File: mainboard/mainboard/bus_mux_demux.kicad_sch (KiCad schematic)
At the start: 10 parts

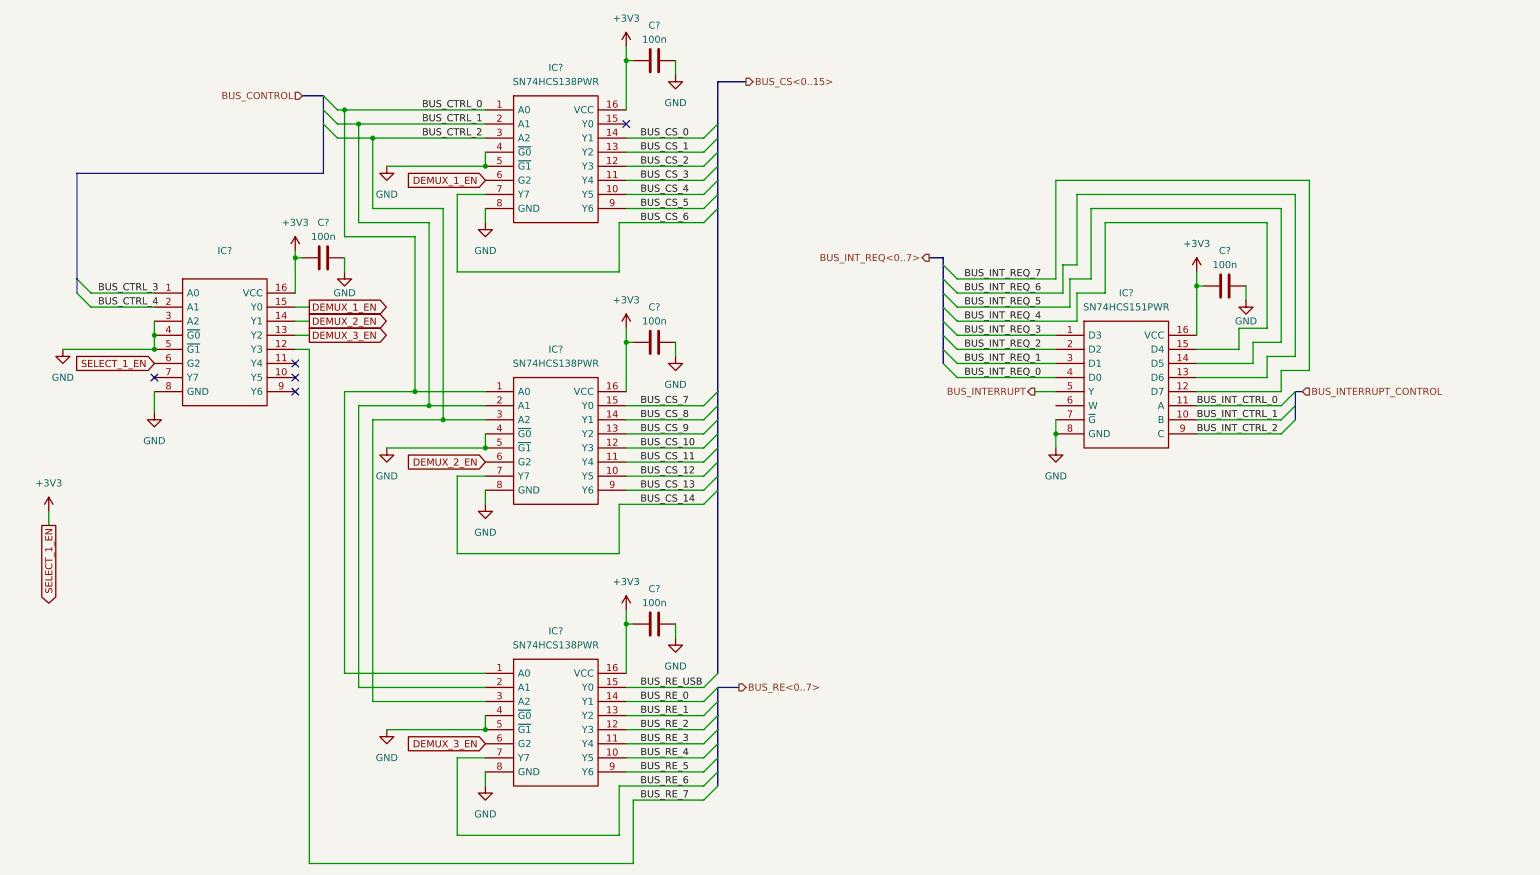
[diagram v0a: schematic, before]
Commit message: Fixing labels
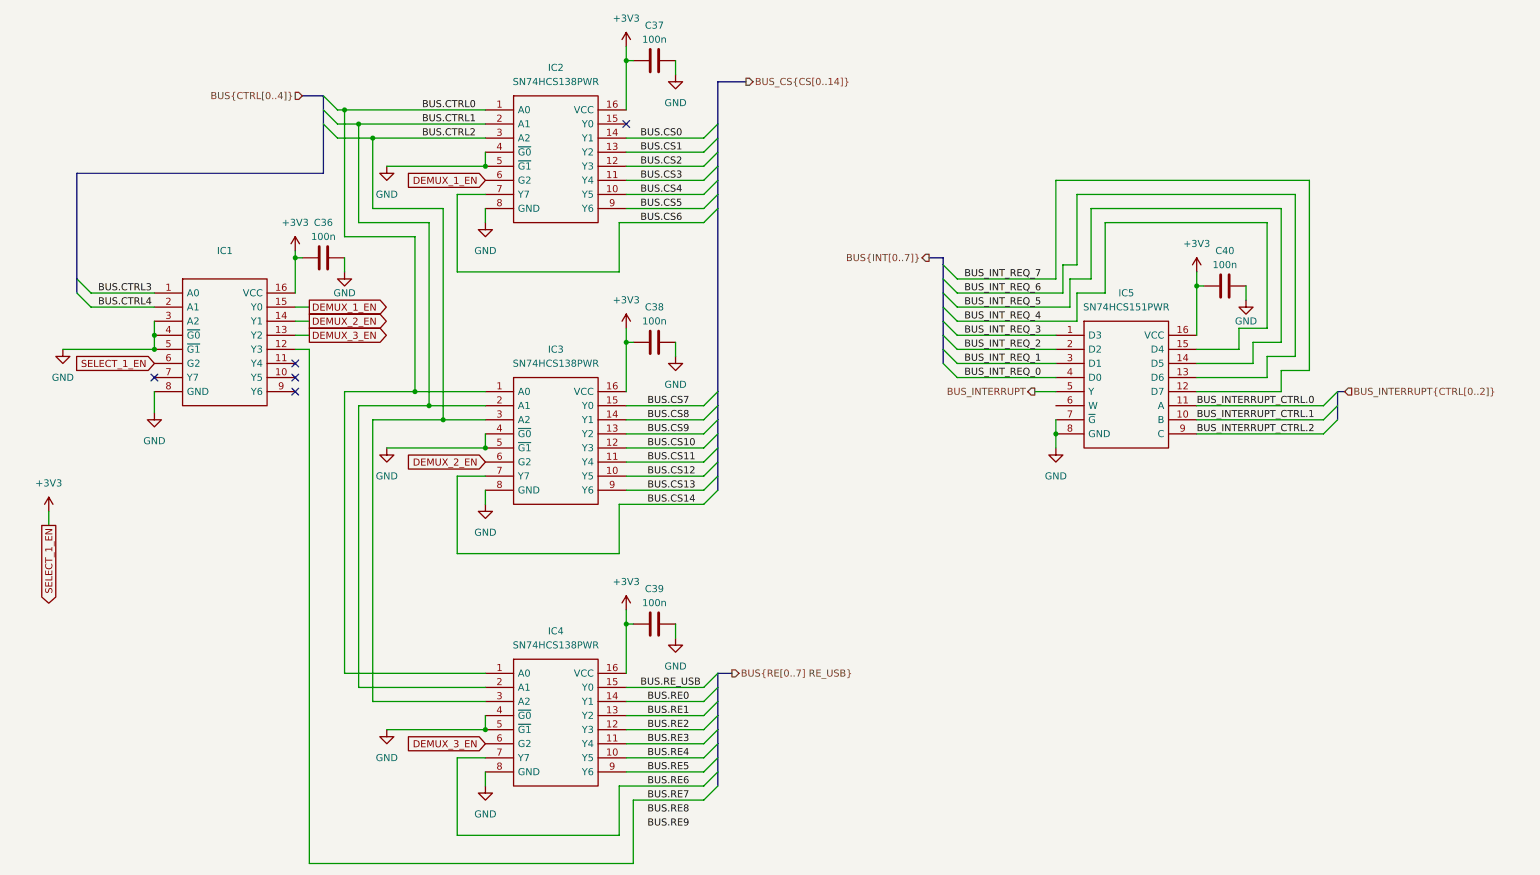
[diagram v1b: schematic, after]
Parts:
- gave numbers to parts that had none: 10
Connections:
- net BUS_CS_0 renamed BUS.CS0
- net BUS_CS_1 renamed BUS.CS1
- net BUS_CS_10 renamed BUS.CS10
- net BUS_CS_11 renamed BUS.CS11
- net BUS_CS_12 renamed BUS.CS12
- net BUS_CS_13 renamed BUS.CS13
- net BUS_CS_14 renamed BUS.CS14
- net BUS_CS_2 renamed BUS.CS2
- net BUS_CS_3 renamed BUS.CS3
- net BUS_CS_4 renamed BUS.CS4
- net BUS_CS_5 renamed BUS.CS5
- net BUS_CS_6 renamed BUS.CS6
- net BUS_CS_7 renamed BUS.CS7
- net BUS_CS_8 renamed BUS.CS8
- net BUS_CS_9 renamed BUS.CS9
- net BUS_CTRL_0 renamed BUS.CTRL0
- net BUS_CTRL_1 renamed BUS.CTRL1
- net BUS_CTRL_2 renamed BUS.CTRL2
- net BUS_CTRL_3 renamed BUS.CTRL3
- net BUS_CTRL_4 renamed BUS.CTRL4
- net BUS_INT_CTRL_0 renamed BUS_INTERRUPT_CTRL.0
- net BUS_INT_CTRL_1 renamed BUS_INTERRUPT_CTRL.1
- net BUS_INT_CTRL_2 renamed BUS_INTERRUPT_CTRL.2
- net BUS_RE_0 renamed BUS.RE0
- net BUS_RE_1 renamed BUS.RE1
- net BUS_RE_2 renamed BUS.RE2
- net BUS_RE_3 renamed BUS.RE3
- net BUS_RE_4 renamed BUS.RE4
- net BUS_RE_5 renamed BUS.RE5
- net BUS_RE_6 renamed BUS.RE6
- net BUS_RE_7 renamed BUS.RE7
- net BUS_RE_USB renamed BUS.RE_USB

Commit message: fixed warnings and errors
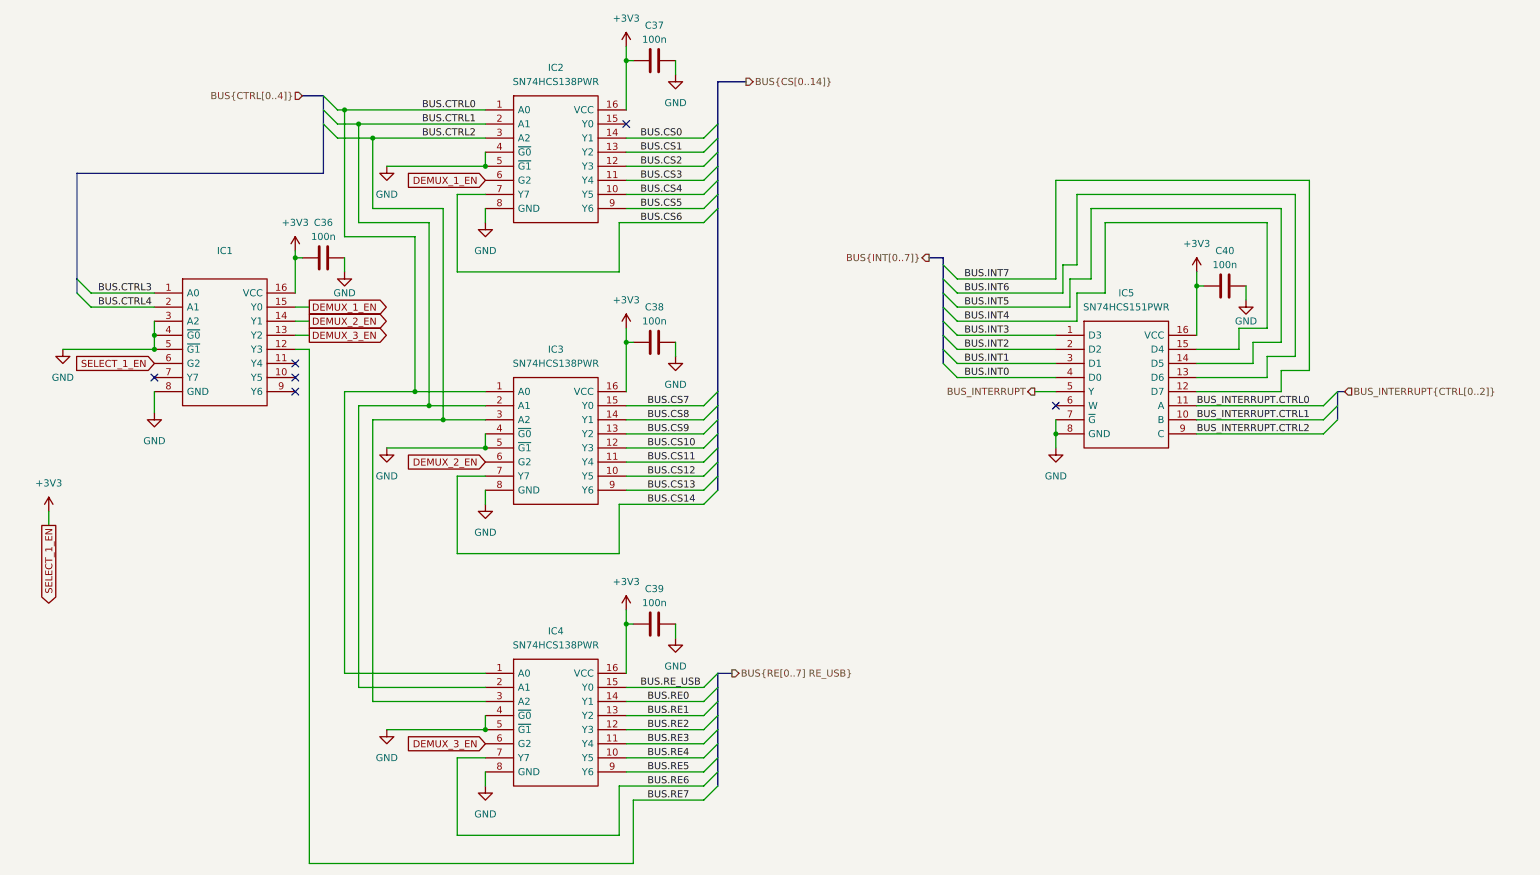
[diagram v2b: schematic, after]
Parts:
- IC1: footprint (none) -> SOP65P640X120-16N
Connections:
- net BUS_INTERRUPT_CTRL.0 renamed BUS_INTERRUPT.CTRL0
- net BUS_INTERRUPT_CTRL.1 renamed BUS_INTERRUPT.CTRL1
- net BUS_INTERRUPT_CTRL.2 renamed BUS_INTERRUPT.CTRL2
- net BUS_INT_REQ_0 renamed BUS.INT0
- net BUS_INT_REQ_1 renamed BUS.INT1
- net BUS_INT_REQ_2 renamed BUS.INT2
- net BUS_INT_REQ_3 renamed BUS.INT3
- net BUS_INT_REQ_4 renamed BUS.INT4
- net BUS_INT_REQ_5 renamed BUS.INT5
- net BUS_INT_REQ_6 renamed BUS.INT6
- net BUS_INT_REQ_7 renamed BUS.INT7
- no-connect marks 5 -> 6
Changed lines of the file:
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@@
   )
   (no_connect (at 132.08 39.37))
+  (no_connect (at 209.55 90.17))
   (no_connect (at 72.39 87.63))
   (no_connect (at 72.39 85.09))
@@
     (stroke (width 0) (type default) (color 0 0 0 0))
   )
-  (label "BUS_INT_REQ_2" (at 193.04 80.01 0)
+  (label "BUS.INT2" (at 193.04 80.01 0)
     (effects (font (size 1.27 1.27)) (justify left bottom))
   )
@@
     (effects (font (size 1.27 1.27)) (justify left bottom))
   )
-  (label "BUS_INT_REQ_4" (at 193.04 74.93 0)
+  (label "BUS.INT4" (at 193.04 74.93 0)
     (effects (font (size 1.27 1.27)) (justify left bottom))
   )
@@
     (effects (font (size 1.27 1.27)) (justify left bottom))
   )
-  (label "BUS_INTERRUPT_CTRL.1" (at 234.95 92.71 0)
-    (effects (font (size 1.27 1.27)) (justify left bottom))
-  )
-  (label "BUS_INT_REQ_1" (at 193.04 82.55 0)
-    (effects (font (size 1.27 1.27)) (justify left bottom))
-  )
-  (label "BUS_INT_REQ_6" (at 193.04 69.85 0)
+  (label "BUS_INTERRUPT.CTRL1" (at 234.95 92.71 0)
+    (effects (font (size 1.27 1.27)) (justify left bottom))
+  )
+  (label "BUS.INT1" (at 193.04 82.55 0)
+    (effects (font (size 1.27 1.27)) (justify left bottom))
+  )
+  (label "BUS.INT6" (at 193.04 69.85 0)
     (effects (font (size 1.27 1.27)) (justify left bottom))
   )
@@
     (effects (font (size 1.27 1.27)) (justify left bottom))
   )
-  (label "BUS_INT_REQ_0" (at 193.04 85.09 0)
+  (label "BUS.INT0" (at 193.04 85.09 0)
     (effects (font (size 1.27 1.27)) (justify left bottom))
   )
@@
     (effects (font (size 1.27 1.27)) (justify left bottom))
   )
-  (label "BUS_INTERRUPT_CTRL.0" (at 234.95 90.17 0)
+  (label "BUS_INTERRUPT.CTRL0" (at 234.95 90.17 0)
     (effects (font (size 1.27 1.27)) (justify left bottom))
   )
@@
     (effects (font (size 1.27 1.27)) (justify left bottom))
   )
-  (label "BUS.RE8" (at 135.89 163.83 0)
-    (effects (font (size 1.27 1.27)) (justify left bottom))
-  )
   (label "BUS.CTRL4" (at 36.83 72.39 0)
     (effects (font (size 1.27 1.27)) (justify left bottom))
@@
     (effects (font (size 1.27 1.27)) (justify left bottom))
   )
-  (label "BUS_INT_REQ_3" (at 193.04 77.47 0)
+  (label "BUS.INT3" (at 193.04 77.47 0)
     (effects (font (size 1.27 1.27)) (justify left bottom))
   )
@@
     (effects (font (size 1.27 1.27)) (justify left bottom))
   )
-  (label "BUS_INTERRUPT_CTRL.2" (at 234.95 95.25 0)
+  (label "BUS_INTERRUPT.CTRL2" (at 234.95 95.25 0)
     (effects (font (size 1.27 1.27)) (justify left bottom))
   )
@@
     (effects (font (size 1.27 1.27)) (justify left bottom))
   )
-  (label "BUS_INT_REQ_7" (at 193.04 67.31 0)
+  (label "BUS.INT7" (at 193.04 67.31 0)
     (effects (font (size 1.27 1.27)) (justify left bottom))
   )
@@
     (effects (font (size 1.27 1.27)) (justify left bottom))
   )
-  (label "BUS.RE9" (at 135.89 166.37 0)
-    (effects (font (size 1.27 1.27)) (justify left bottom))
-  )
   (label "BUS.RE_USB" (at 134.62 140.97 0)
     (effects (font (size 1.27 1.27)) (justify left bottom))
   )
-  (label "BUS_INT_REQ_5" (at 193.04 72.39 0)
+  (label "BUS.INT5" (at 193.04 72.39 0)
     (effects (font (size 1.27 1.27)) (justify left bottom))
   )
@@
     (effects (font (size 1.27 1.27)) (justify left))
   )
-  (hierarchical_label "BUS_CS{CS[0..14]}" (shape output) (at 153.67 31.75 0)
+  (hierarchical_label "BUS{CS[0..14]}" (shape output) (at 153.67 31.75 0)
     (effects (font (size 1.27 1.27)) (justify left))
   )
@@
     (property "Reference" "IC1" (id 0) (at 59.69 62.23 0))
     (property "Value" "~" (id 1) (at 59.69 64.77 0))
-    (property "Footprint" "" (id 2) (at 68.58 67.31 0)
-      (effects (font (size 1.27 1.27)) (justify left) hide)
-    )
+    (property "Footprint" "SOP65P640X120-16N" (id 2) (at 68.58 67.31 0)
+      (effects (font (size 1.27 1.27)) (justify left) hide)
+    )

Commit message: board almost ready, paths must be aligned
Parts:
- C501: renamed from C36; footprint Capacitor_SMD:C_0402_1005Metric_Pad0.74x0.62mm_HandSolder -> Capacitor_SMD:C_0603_1608Metric_Pad1.08x0.95mm_HandSolder
- C502: renamed from C37; footprint Capacitor_SMD:C_0402_1005Metric_Pad0.74x0.62mm_HandSolder -> Capacitor_SMD:C_0603_1608Metric_Pad1.08x0.95mm_HandSolder
- C503: renamed from C38; footprint Capacitor_SMD:C_0402_1005Metric_Pad0.74x0.62mm_HandSolder -> Capacitor_SMD:C_0603_1608Metric_Pad1.08x0.95mm_HandSolder
- C504: renamed from C39; footprint Capacitor_SMD:C_0402_1005Metric_Pad0.74x0.62mm_HandSolder -> Capacitor_SMD:C_0603_1608Metric_Pad1.08x0.95mm_HandSolder
- C505: renamed from C40; footprint Capacitor_SMD:C_0402_1005Metric_Pad0.74x0.62mm_HandSolder -> Capacitor_SMD:C_0603_1608Metric_Pad1.08x0.95mm_HandSolder
- IC501: renamed from IC1; value ~ -> SN74HCS138PWR
- renumbered IC2 to IC502, IC3 to IC503, IC4 to IC504, IC5 to IC505
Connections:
- net BUS.CS10: now also IC504.15 (Y0); no longer IC503.12 (Y3)
- net BUS.CS11: now also IC504.14 (Y1); no longer IC503.11 (Y4)
- net BUS.CS12: now also IC504.12 (Y3); no longer IC503.10 (Y5)
- net BUS.CS13: now also IC504.11 (Y4); no longer IC503.9 (Y6)
- net BUS.CS14: now also IC504.9 (Y6); no longer IC503.7 (Y7)
- net BUS.CS2: now also IC502.11 (Y4); no longer IC502.12 (Y3)
- net BUS.CS3: now also IC502.10 (Y5); no longer IC502.11 (Y4)
- net BUS.CS4: now also IC502.7 (Y7); no longer IC502.10 (Y5)
- net BUS.CS5: now also IC503.15 (Y0); no longer IC502.9 (Y6)
- net BUS.CS6: now also IC503.13 (Y2); no longer IC502.7 (Y7)
- net BUS.CS7: now also IC503.12 (Y3); no longer IC503.15 (Y0)
- net BUS.CS8: now also IC503.10 (Y5); no longer IC503.14 (Y1)
- net BUS.CS9: now also IC503.9 (Y6); no longer IC503.13 (Y2)
- net BUS.RE0: now also IC502.12 (Y3); no longer IC504.14 (Y1)
- net BUS.RE1: now also IC502.9 (Y6); no longer IC504.13 (Y2)
- net BUS.RE2: now also IC503.14 (Y1); no longer IC504.12 (Y3)
- net BUS.RE3: now also IC503.11 (Y4); no longer IC504.11 (Y4)
- net BUS.RE4: now also IC503.7 (Y7); no longer IC504.10 (Y5)
- net BUS.RE5: now also IC504.13 (Y2); no longer IC504.9 (Y6)
- net BUS.RE6: now also IC504.10 (Y5); no longer IC504.7 (Y7)
- net BUS.RE7: now also IC504.7 (Y7); no longer IC501.12 (Y3)
- net BUS.RE_USB: now also IC501.12 (Y3); no longer IC504.15 (Y0)

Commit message: motherboard designed
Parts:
- U: renamed from IC502; value SN74HCS138PWR -> (none); footprint SOP65P640X120-16N -> (none)
- U: renamed from IC501; value SN74HCS138PWR -> (none); footprint SOP65P640X120-16N -> (none)
- U: renamed from C502; value 100n -> (none); footprint Capacitor_SMD:C_0603_1608Metric_Pad1.08x0.95mm_HandSolder -> (none)
- U: renamed from IC503; value SN74HCS138PWR -> (none); footprint SOP65P640X120-16N -> (none)
- U: renamed from IC505; value SN74HCS151PWR -> (none); footprint SOP65P640X120-16N -> (none)
- U: renamed from C505; value 100n -> (none); footprint Capacitor_SMD:C_0603_1608Metric_Pad1.08x0.95mm_HandSolder -> (none)
- U: renamed from IC504; value SN74HCS138PWR -> (none); footprint SOP65P640X120-16N -> (none)
- U: renamed from C501; value 100n -> (none); footprint Capacitor_SMD:C_0603_1608Metric_Pad1.08x0.95mm_HandSolder -> (none)
- U: renamed from C504; value 100n -> (none); footprint Capacitor_SMD:C_0603_1608Metric_Pad1.08x0.95mm_HandSolder -> (none)
- U: renamed from C503; value 100n -> (none); footprint Capacitor_SMD:C_0603_1608Metric_Pad1.08x0.95mm_HandSolder -> (none)

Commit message: schematic for gpu extension
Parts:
- C501, C502, C503, C504, C505: renamed from U; value (none) -> 100n; footprint (none) -> Capacitor_SMD:C_0603_1608Metric_Pad1.08x0.95mm_HandSolder
- IC501, IC502, IC503, IC504: renamed from U; value (none) -> SN74HCS138PWR; footprint (none) -> footprints:SOP65P640X120-16N
- IC505: renamed from U; value (none) -> SN74HCS151PWR; footprint (none) -> footprints:SOP65P640X120-16N

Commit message: some ERC fixes
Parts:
- IC501, IC502, IC503, IC504, IC505: footprint footprints:SOP65P640X120-16N -> SOP65P640X120-16N
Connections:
- net BUS.CS14: no longer names the net of IC504.9 (Y6)
- net BUS.RE_USB: no longer names the net of IC501.12 (Y3)
- no-connect marks 6 -> 8

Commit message: some fixes for ERC
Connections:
- net BUS.INT7: no longer names the net of IC505.12 (D7)
- net BUS.RE7: no longer names the net of IC504.7 (Y7)
- no-connect marks 8 -> 10
